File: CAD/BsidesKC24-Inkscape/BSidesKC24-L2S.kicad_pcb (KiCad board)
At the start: 2 copper layers, 63.5 x 99 mm, 11 parts, among them SW1 SW_SPST

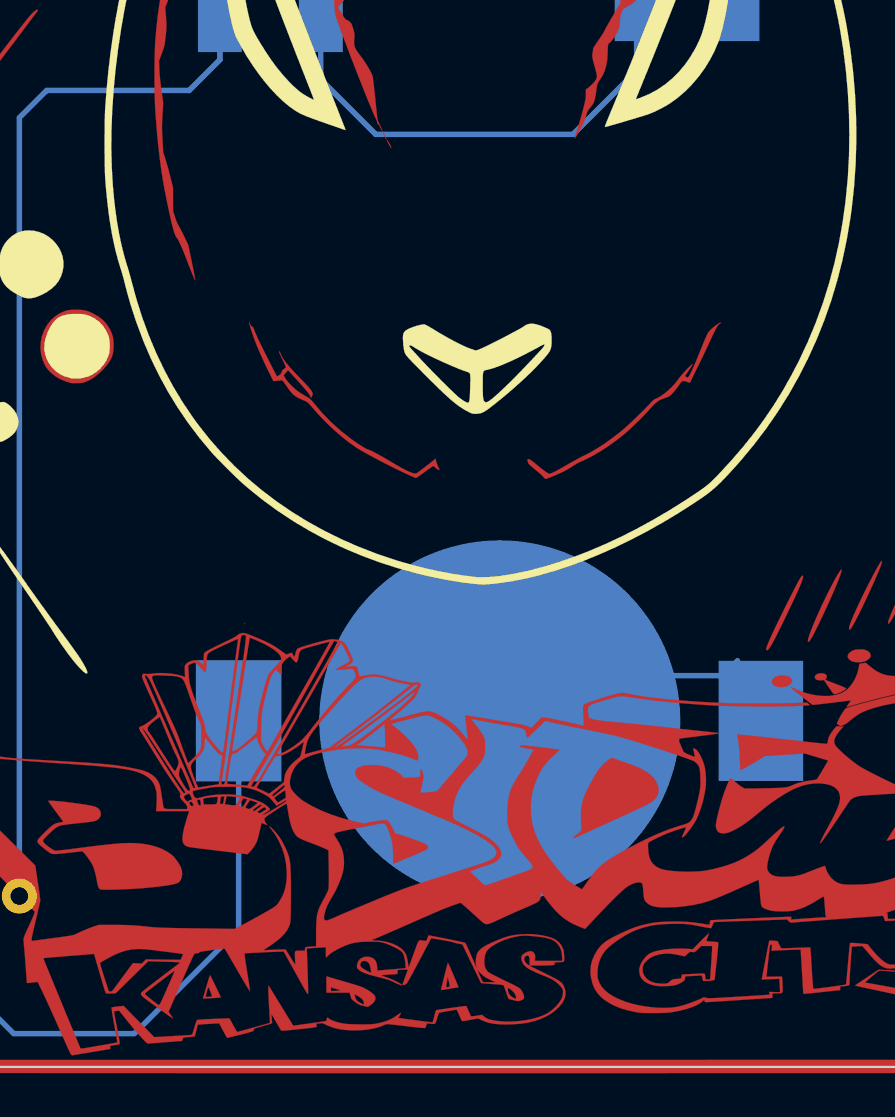
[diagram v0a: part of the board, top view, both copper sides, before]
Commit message: Updated circuit
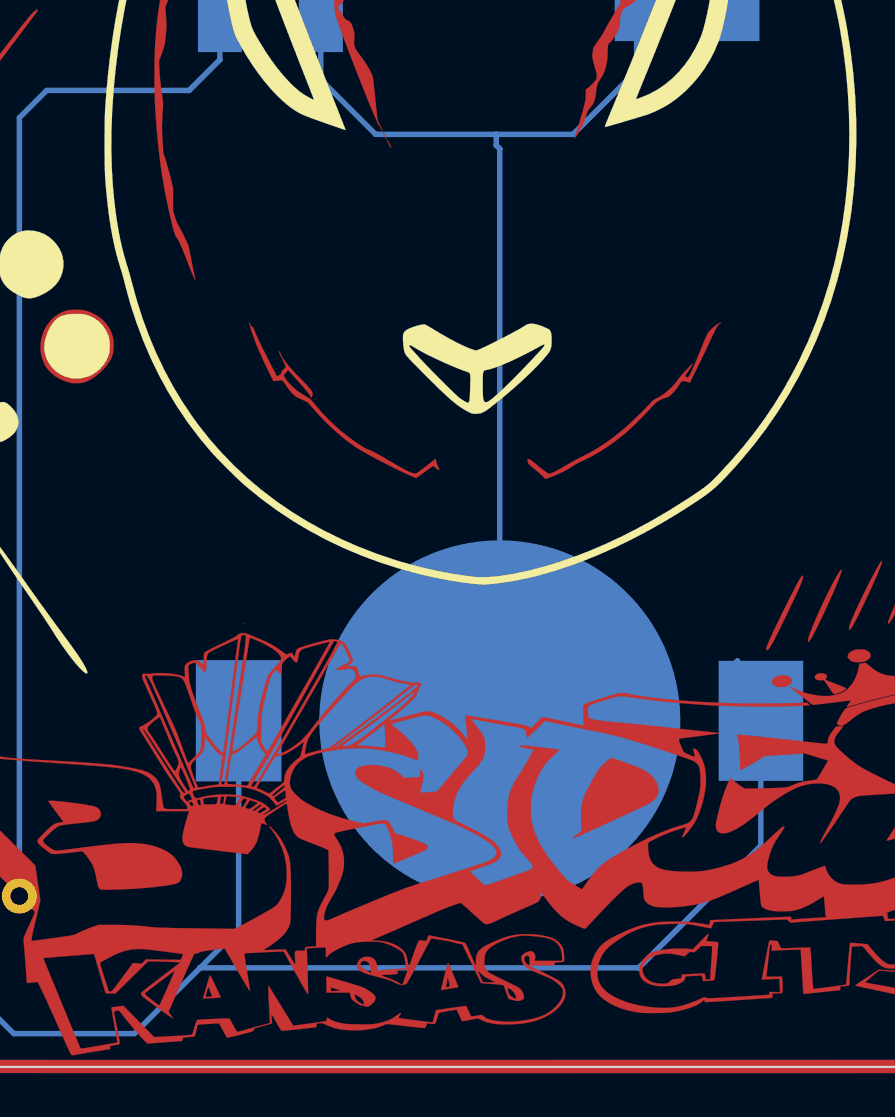
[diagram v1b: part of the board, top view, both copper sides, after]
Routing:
- net Net-(BT1-+): track 33.5 -> 63.5 mm
- net GND: track 21.7 -> 48.5 mm

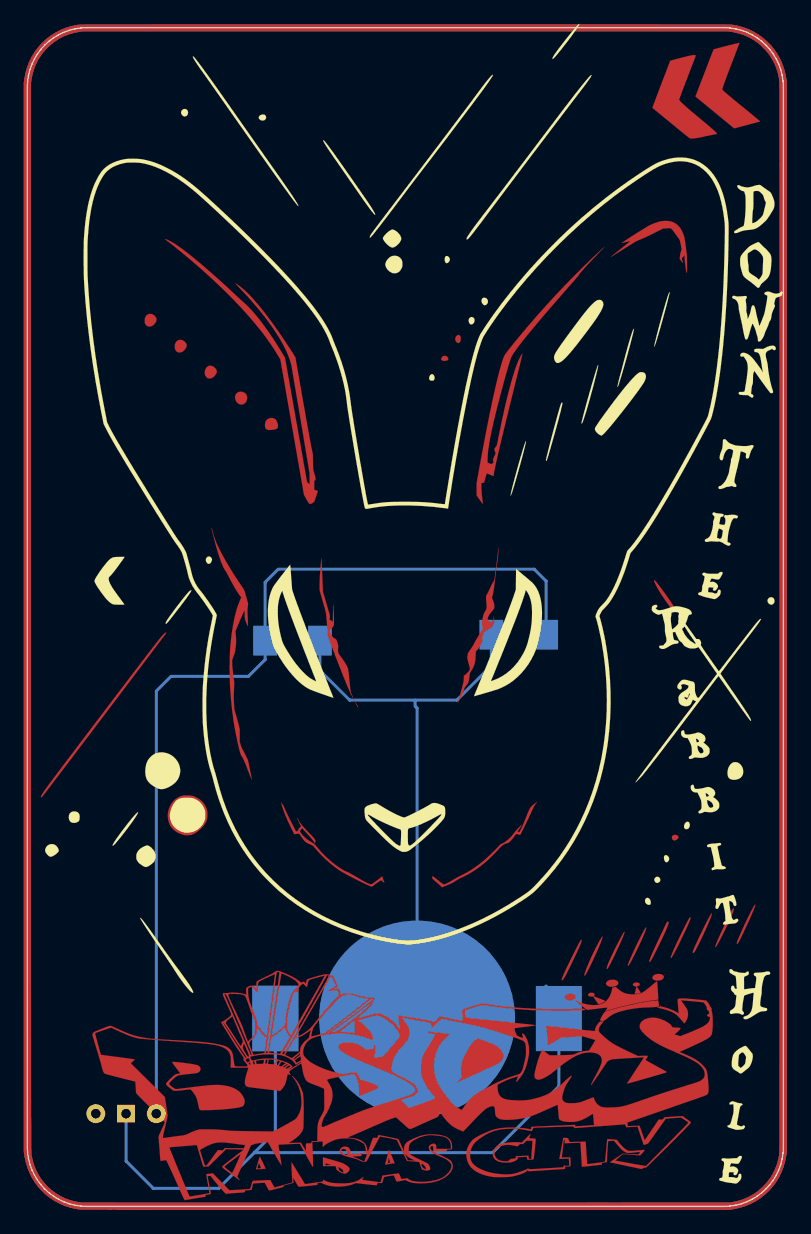
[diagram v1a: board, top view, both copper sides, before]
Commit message: Moved switch to avoid front copper
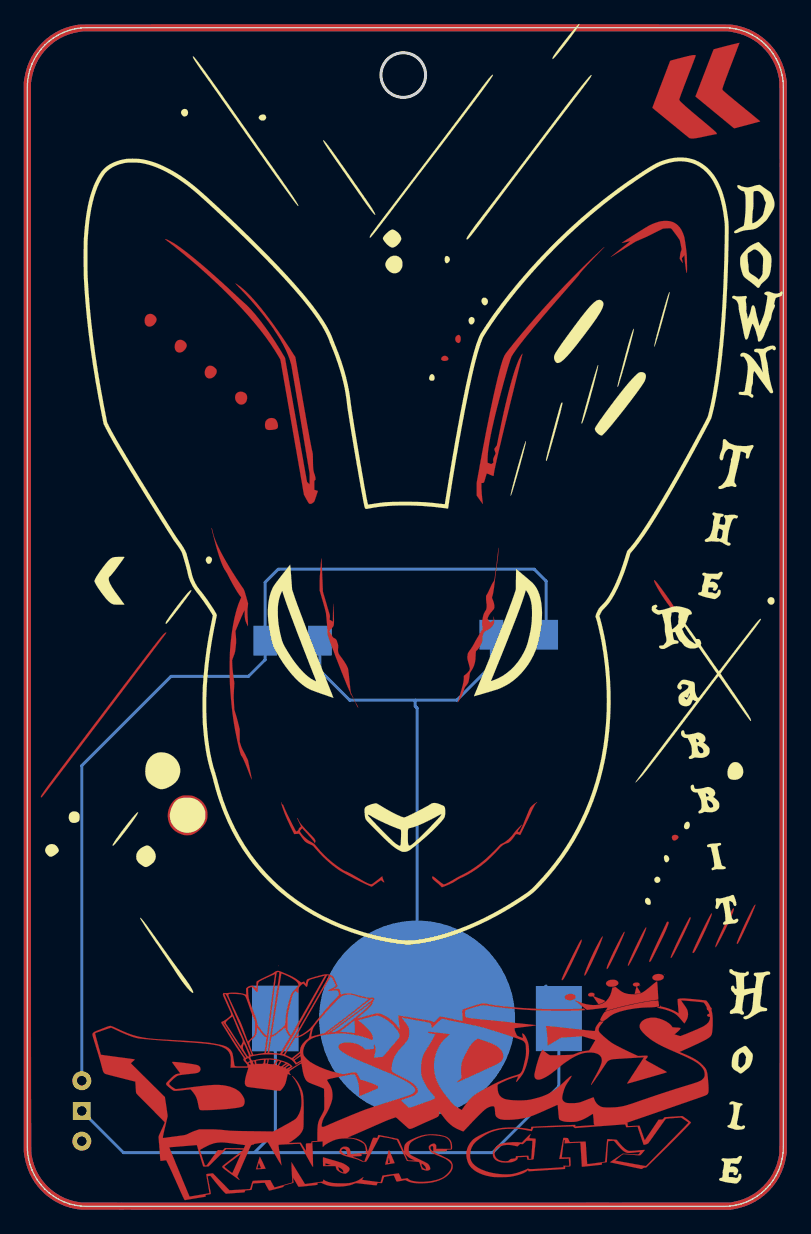
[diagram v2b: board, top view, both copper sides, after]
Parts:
- moved SW1 3.72 mm to (63.0, 145.0), turned to -90 degrees
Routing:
- net Net-(BT1-+): track 63.5 -> 62.5 mm
- net (no net): vias 0 -> 1
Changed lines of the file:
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@@
 	(footprint "Button_Switch_THT:SW_Slide-03_Wuerth-WS-SLTV_10x2.5x6.4_P2.54mm"
 		(layer "B.Cu")
-		(at 66.717457 145.228002 180)
+		(at 63 145 -90)
 		(descr "Wuerth, WS-SLTV, 450301014042, https://www.we-online.com/components/products/datasheet/450301014042.pdf")
 		(tags "switch single-pole double-throw SPDT würth wurth")
 		(property "Reference" "SW1"
-			(at 0 2.54 180)
+			(at 0 2.54 90)
 			(layer "B.SilkS")
 			(effects
@@
 		)
 		(property "Value" "SW_SPST"
-			(at 0 -3.81 180)
+			(at 0 -3.81 90)
 			(layer "B.Fab")
 			(effects
@@
 		)
 		(property "Footprint" "Button_Switch_THT:SW_Slide-03_Wuerth-WS-SLTV_10x2.5x6.4_P2.54mm"
-			(at 0 0 0)
+			(at 0 0 90)
 			(unlocked yes)
 			(layer "B.Fab")
@@
 		)
 		(property "Datasheet" ""
-			(at 0 0 0)
+			(at 0 0 90)
 			(unlocked yes)
 			(layer "B.Fab")
@@
 		)
 		(property "Description" "Single Pole Single Throw (SPST) switch"
-			(at 0 0 0)
+			(at 0 0 90)
 			(unlocked yes)
 			(layer "B.Fab")
@@
 		)
 		(fp_text user "${REFERENCE}"
-			(at 0 -2.54 180)
+			(at 0 -2.54 90)
 			(layer "B.Fab")
 			(effects
@@
 		)
 		(pad "1" thru_hole rect
-			(at 0 0 180)
+			(at 0 0 270)
 			(size 1.5 1.5)
 			(drill 0.8)
@@
 		)
 		(pad "2" thru_hole circle
-			(at -2.54 0 180)
+			(at -2.54 0 270)
 			(size 1.6 1.6)
 			(drill 0.8)
@@
 		)
 		(pad "3" thru_hole circle
-			(at 2.54 0 180)
+			(at 2.54 0 270)
 			(size 1.6 1.6)
 			(drill 0.8)
@@
 		(layer "Edge.Cuts")
 	)
+	(via
+		(at 90 58)
+		(size 4)
+		(drill 3.5)
+		(layers "F.Cu" "B.Cu")
+		(net 0)
+	)
+	(segment
+		(start 103.065705 142.934295)
+		(end 103.065705 137.240877)
+		(width 0.25)
+		(layer "B.Cu")
+		(net 1)
+	)
 	(segment
 		(start 79.255705 146.744295)
@@
 	)
 	(segment
-		(start 69 151.5)
-		(end 66.717457 149.217457)
-		(width 0.25)
-		(layer "B.Cu")
-		(net 1)
-	)
-	(segment
-		(start 77.5 148.5)
-		(end 74.5 151.5)
-		(width 0.25)
-		(layer "B.Cu")
-		(net 1)
-	)
-	(segment
-		(start 74.5 151.5)
-		(end 69 151.5)
-		(width 0.25)
-		(layer "B.Cu")
-		(net 1)
-	)
-	(segment
-		(start 97.5 148.5)
-		(end 77.5 148.5)
-		(width 0.25)
-		(layer "B.Cu")
-		(net 1)
-	)
-	(segment
-		(start 103.065705 137.240877)
-		(end 103.065705 142.934295)
-		(width 0.25)
-		(layer "B.Cu")
-		(net 1)
-	)
-	(segment
-		(start 66.717457 149.217457)
-		(end 66.717457 145.228002)
-		(width 0.25)
-		(layer "B.Cu")
-		(net 1)
-	)
-	(segment
 		(start 102 134.5)
 		(end 101.320053 135.179947)
@@
 	)
 	(segment
+		(start 97.5 148.5)
+		(end 103.065705 142.934295)
+		(width 0.25)
+		(layer "B.Cu")
+		(net 1)
+	)
+	(segment
+		(start 77.5 148.5)
+		(end 97.5 148.5)
+		(width 0.25)
+		(layer "B.Cu")
+		(net 1)
+	)
+	(segment
+		(start 77.5 148.5)
+		(end 66.5 148.5)
+		(width 0.25)
+		(layer "B.Cu")
+		(net 1)
+	)
+	(segment
 		(start 79.255705 137.240877)
 		(end 79.255705 146.744295)
@@
 	)
 	(segment
-		(start 103.065705 142.934295)
-		(end 97.5 148.5)
+		(start 66.5 148.5)
+		(end 63 145)
 		(width 0.25)
 		(layer "B.Cu")
@@
 	)
 	(segment
-		(start 70.5 108.5)
-		(end 69.257457 109.742543)
-		(width 0.25)
-		(layer "B.Cu")
-		(net 3)
-	)
-	(segment
 		(start 78.4 105.5)
 		(end 78.4 107.1)
@@
 	)
 	(segment
-		(start 69.257457 109.742543)
-		(end 69.257457 145.228002)
-		(width 0.25)
-		(layer "B.Cu")
-		(net 3)
-	)
-	(segment
 		(start 101 99.5)
 		(end 102 100.5)
@@
 	)
 	(segment
+		(start 63 142.46)
+		(end 63 116)
+		(width 0.25)
+		(layer "B.Cu")
+		(net 3)
+	)
+	(segment
 		(start 102 100.5)
 		(end 102 105)
 		(width 0.25)
 		(layer "B.Cu")
+		(net 3)
+	)
+	(segment
+		(start 63 116)
+		(end 70.5 108.5)
+		(width 0.25)
+		(layer "B.Cu")

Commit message: Added BP logos
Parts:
- added G***: BP Logo, _BadgePirates_Logo:BPSkull_Distressed_B.SILK, F.Cu at (90.0, 67.0)
- added G***: fg, _BadgePirates_Logo:FG_B.SILK, F.Cu at (114.0, 120.0)
- added G***: NG_BSilk, _BadgePirates_Logo:NG_B.SLK, F.Cu at (114.0, 146.0)
- added G***: Rixon, _BadgePirates_Logo:rixon_B.SLK, F.Cu at (114.0, 135.0)
